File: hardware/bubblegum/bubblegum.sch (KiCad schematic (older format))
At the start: 136 parts, among them P1 RX_OUT, P2 RX_ONLY, P3 SERIAL, P4 TX/RX, P5 CONN_2, P6 TX_IN, P7 VCC, P8 SWITCH_CTRL, T1 RX_IF_BALUN, T2 RX_BALUN, T4 TX_BALUN, T6 TX_IF_BALUN, U1 DMN2400, U10 TX_HIGHPASS_FILTER, U11 PE4140, U12 SKY13350, U13 TX_LOWPASS_FILTER, U14 DMC2400, U15 DMC2400, U16 GSG-74HC04, U17 SKY13350, U18 DMN2400, U19 NCP699, U2 SKY13350, U3 RX_HIGHPASS_FILTER, U4 SKY13350, U5 SKY13350, U6 PE4140, U7 RX_LOWPASS_FILTER, U8 SKY13350, U9 TRF3765

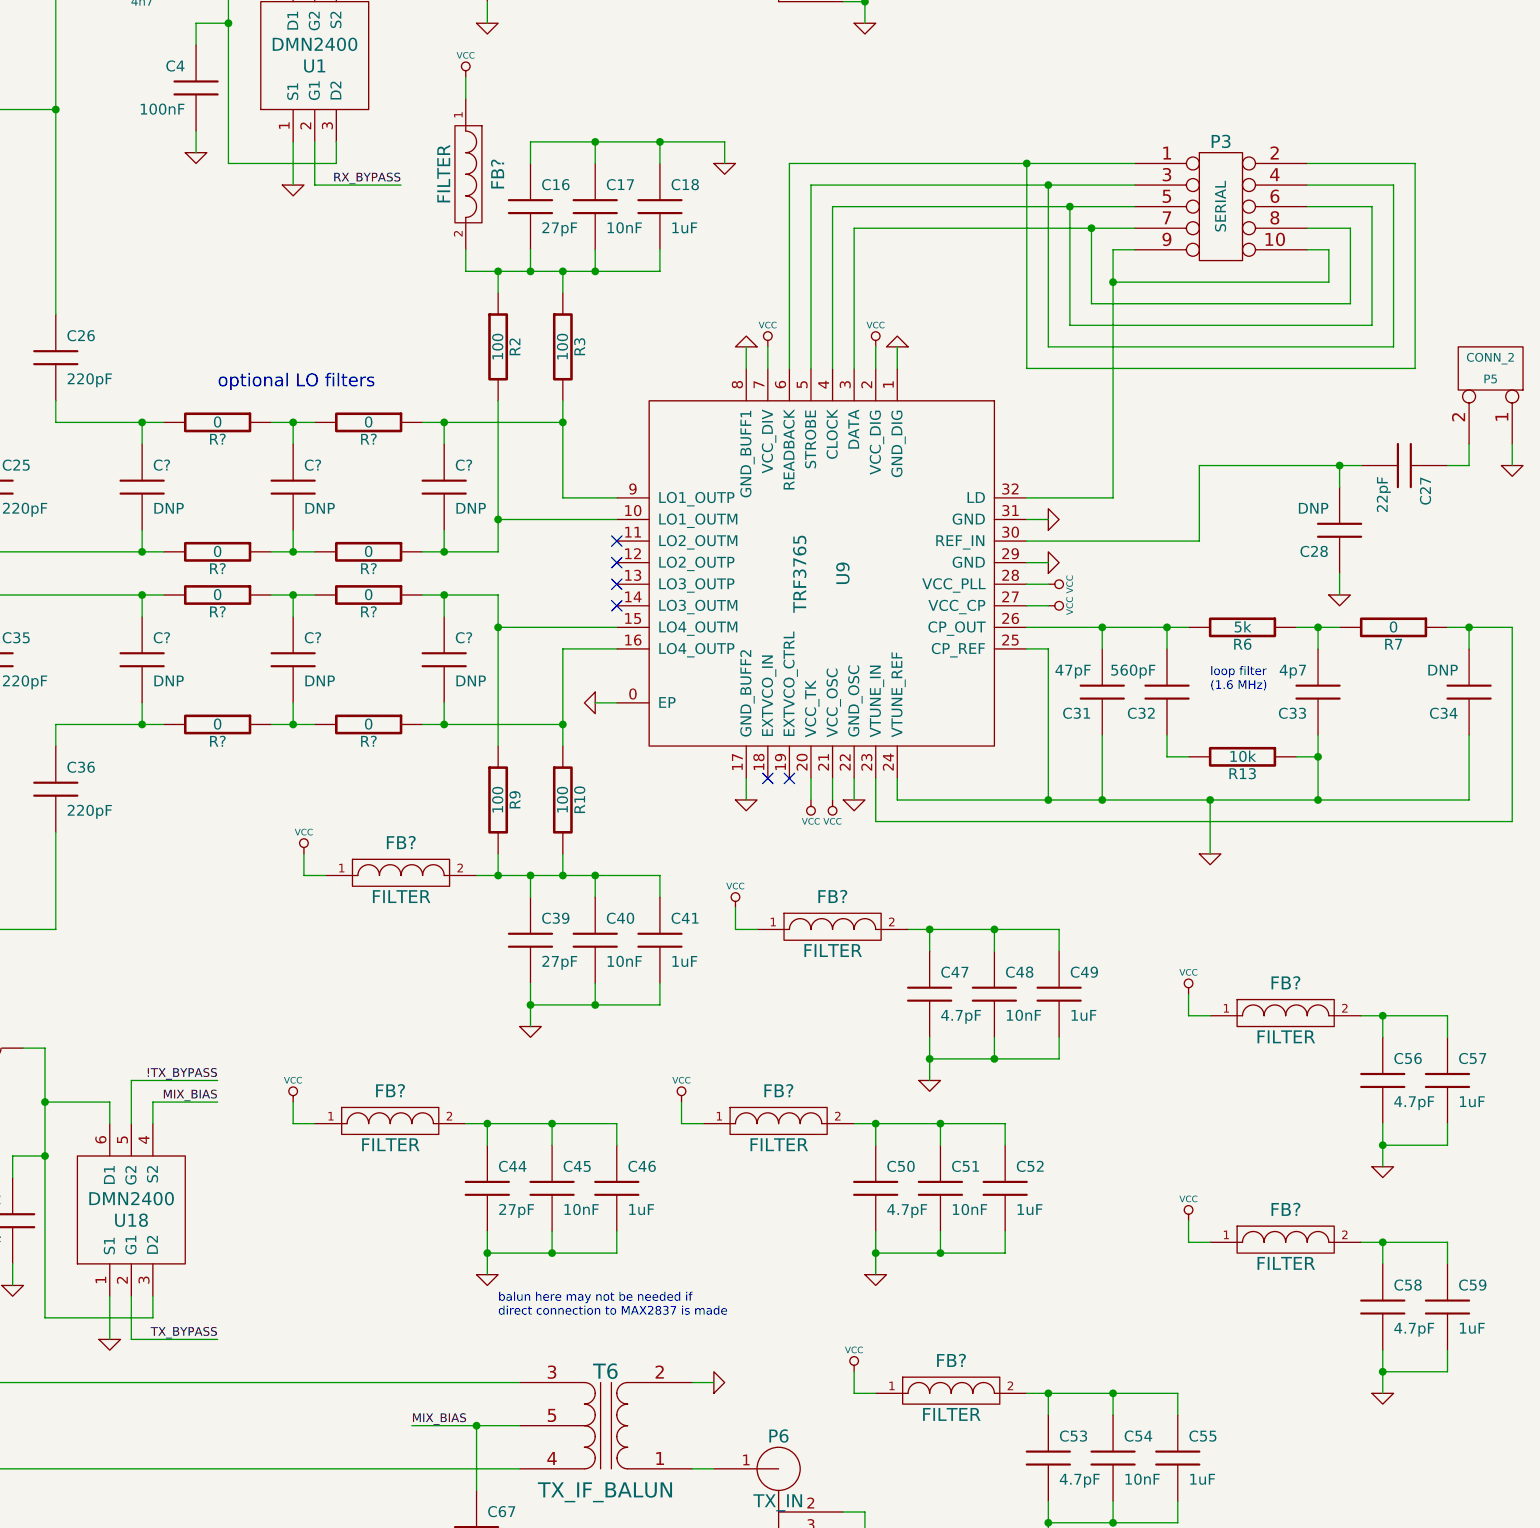
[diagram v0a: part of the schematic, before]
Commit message: started module selection, Anaren balun module
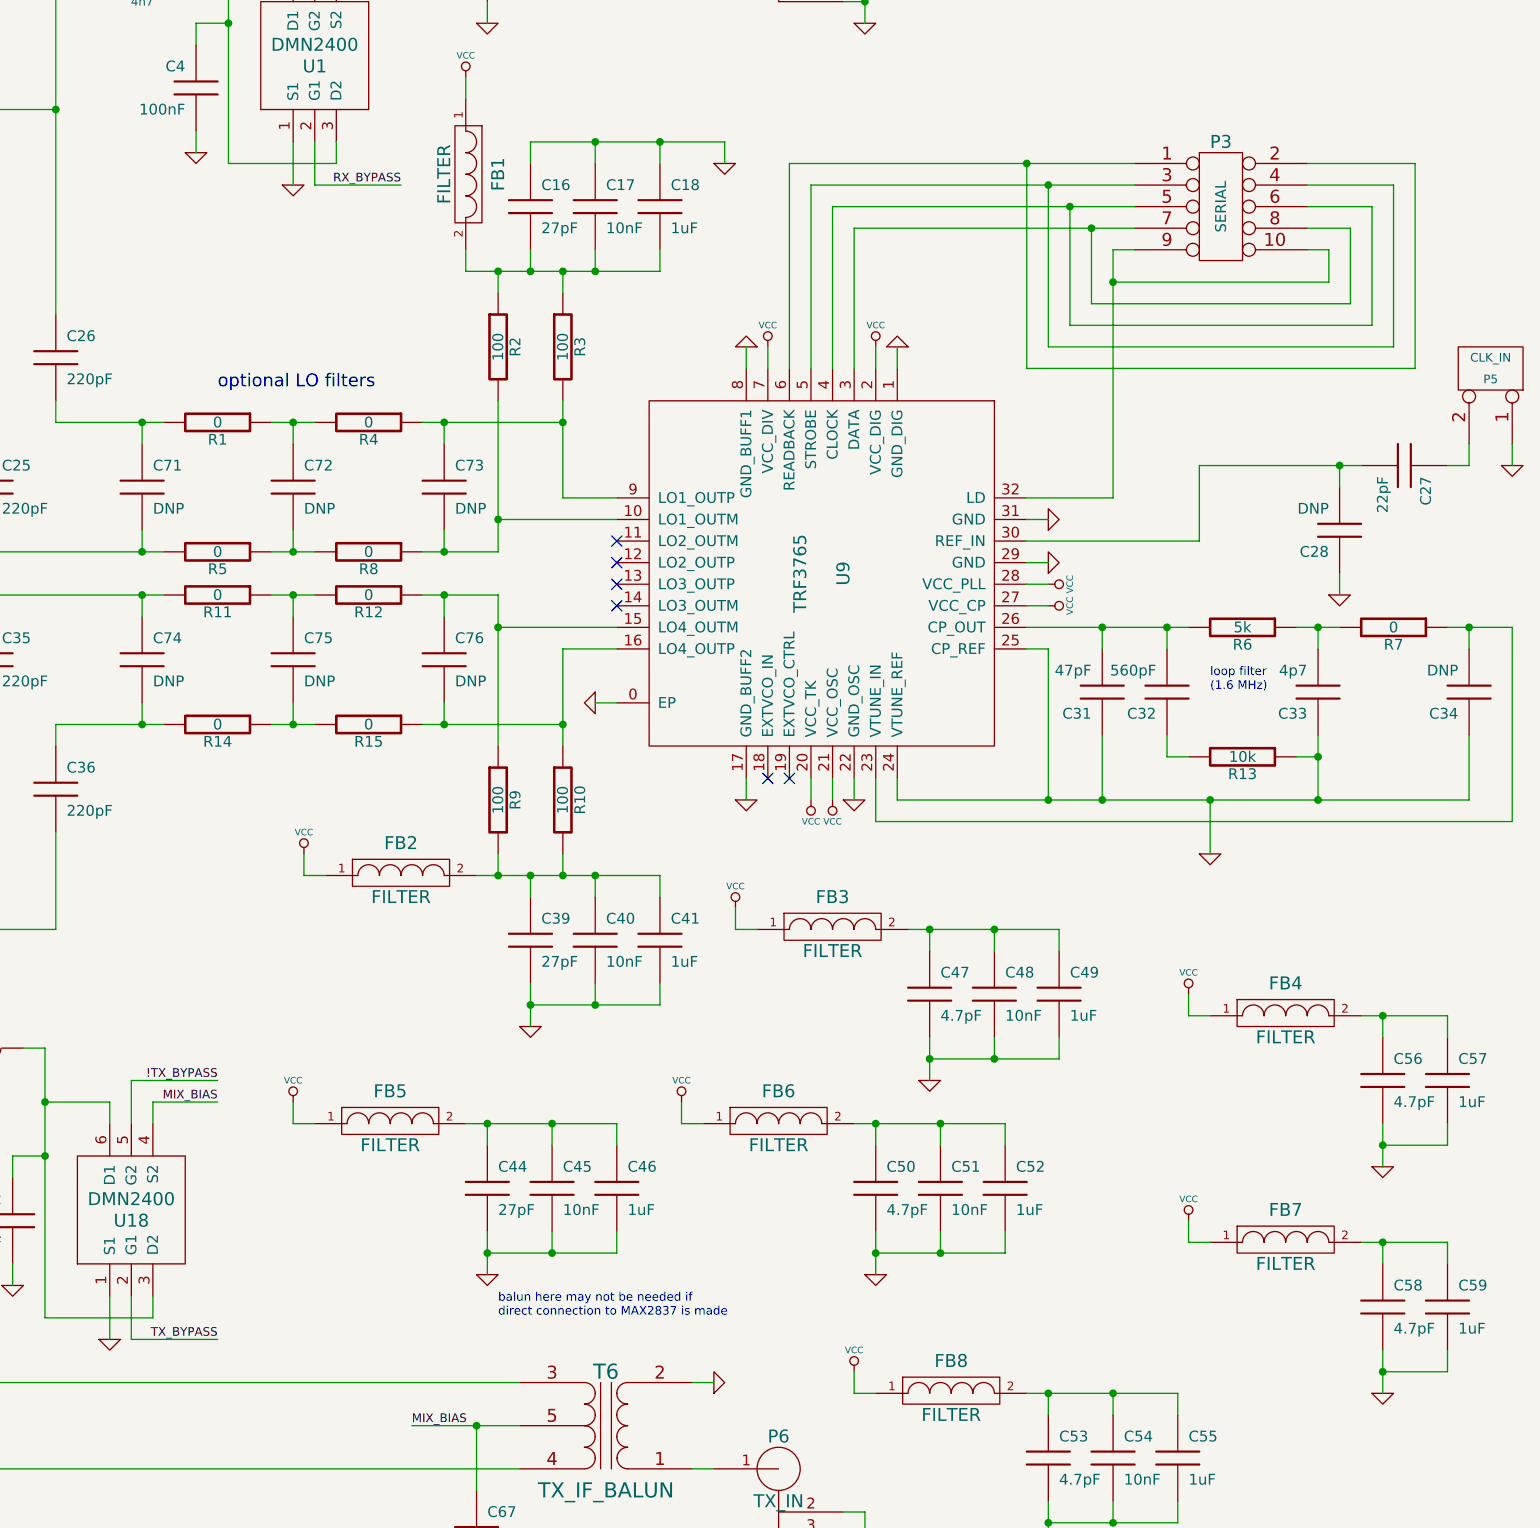
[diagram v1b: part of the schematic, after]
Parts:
- P5: value CONN_2 -> CLK_IN
- T1, T6: Description (none) -> BALUN CERAMIC CHIP WIMAX 2.5GHZ; Manufacturer (none) -> Johanson Technology; Part Number (none) -> 2500BL14M100T
- gave numbers to parts that had none: 22

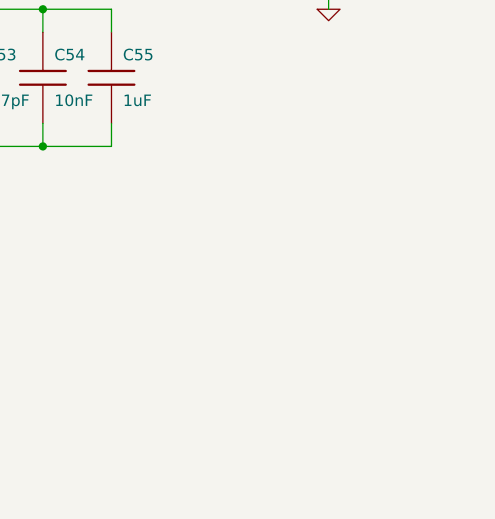
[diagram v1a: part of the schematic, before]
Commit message: mounting holes
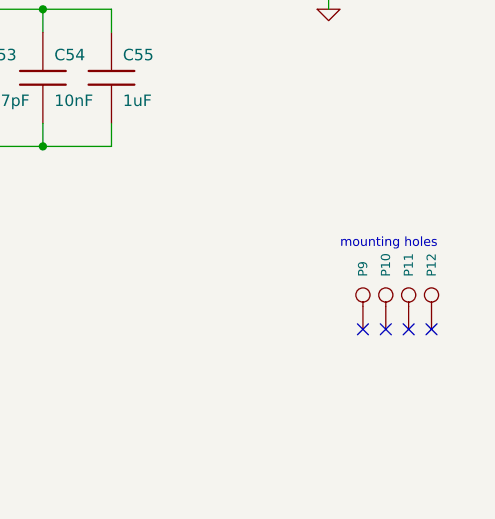
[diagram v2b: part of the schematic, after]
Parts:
- added P10, P11, P12, P9: CONN_1, symbol CONN_1
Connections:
- no-connect marks 7 -> 11
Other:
- note added: "mounting holes"

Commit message: fixed TRF3765 supply connections
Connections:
- net VCC: no longer U9.2 (VCC_DIG), U9.20 (VCC_TK), U9.21 (VCC_OSC), U9.27 (VCC_CP), U9.28 (VCC_PLL), U9.7 (VCC_DIV)
- net VCC_DIG: now reaches C44.1, C45.1, C46.1, FB5.2
- net VCC_DIG: now also U9.2 (VCC_DIG)
- net VCC_DIV: now reaches C47.1, C48.1, C49.1, FB3.2
- net VCC_DIV: now also U9.7 (VCC_DIV)
- net VCC_TK: now reaches C50.1, C51.1, C52.1, FB6.2
- net VCC_TK: now also U9.20 (VCC_TK)
- net VCC_CP: now reaches C58.1, C59.1, FB7.2
- net VCC_CP: now also U9.27 (VCC_CP)
- net VCC_PLL: now reaches C56.1, C57.1, FB4.2
- net VCC_PLL: now also U9.28 (VCC_PLL)
- net VCC_OSC: now reaches C53.1, C54.1, C55.1, FB8.2
- net VCC_OSC: now also U9.21 (VCC_OSC)
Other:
- moved on the sheet: C44, C45, C46, FB5

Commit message: switchable TX LO LPF
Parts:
- removed C74, C75, C76: DNP, symbol C
- removed R11, R12, R14, R15: 0, symbol R
- added C? (x4): 220pF, symbol C
- added C? (x2): 33pF, symbol C
- added T?: TX_LO_BALUN1, symbol BALUN-B0310J50100AHF
- added T?: TX_LO_BALUN2, symbol BALUN-B0310J50100AHF
- added U?: TX_LO_FILTER, symbol FIL-DEA
- added U?: SKY13411, symbol SKY13411
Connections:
- net GND: now also C?.2, C?.2, T?.1 (S1), T?.2 (S2), U?.0 (GND), U?.2 (GND), U?.4 (GND)
- net at R9.1, U9.15 (LO4_OUTM): now also C?.2
- net at R10.1, U9.16 (LO4_OUTP): now also C?.2
- net at C35.1: now also T?.3 (PR1)
- net at C36.1: now also T?.4 (PR2)
- new net: T?.1 (S1), U?.4 (TX)
- new net: C?.1, T?.3 (PR1)
- new net: C?.1, T?.4 (PR2)
- new net: C?.2, U?.1 (IN)
- new net: C?.1, U?.3 (OUT)
- new net: T?.2 (S2), U?.6 (ANT1)
- new net: C?.1, U?.1 (ANT2)
- new net: C?.2, U?.3 (RX)
- new net !TX_LO_LPF: C?.1, U?.2 (V2)
- new net TX_LO_LPF: C?.1, U?.5 (V1)
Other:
- moved on the sheet: C1, C10, C11, C12, C13, C15, C2, C20, C23, C24, C35, C36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

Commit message: finished switchable LO LPFs in schematic
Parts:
- removed P8: SWITCH_CTRL, symbol CONN_5X2
- removed R1, R4, R5, R8: 0, symbol R
- added C74: 33pF, symbol C
- added C75, C76: 220pF, symbol C
- added P8: SWITCH_CTRL, symbol CONN_7X2
- added T3: RX_LO_BALUN2, symbol BALUN-B0310J50100AHF
- added T5: RX_LO_BALUN1, symbol BALUN-B0310J50100AHF
- added U20: RX_LO_FILTER, symbol FIL-DEA
- added U21: SKY13411, symbol SKY13411
- C71, C72: value DNP -> 220pF
- C73: value DNP -> 33pF
- gave numbers to parts that had none: 10
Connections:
- net !TX_LO_LPF is gone; now on net !LO_LPF: C80.1, U22.2 (V2)
- net GND: now also C73.2, C74.2, P8.10, P8.12, P8.14, P8.2 (P2), P8.4 (P4), P8.6 (P6), P8.8 (P8), T3.1 (S1), T5.2 (S2), U20.2 (GND), U20.4 (GND), U21.0 (GND)
- net RX_BYPASS: now also P8.1 (P1)
- net RX_HP: now also P8.5 (P5)
- net TX_ANT: now also P8.9
- net TX_BYPASS: now also P8.3 (P3)
- net TX_HP: now also P8.7 (P7)
- net VCC: now also P8.13; no longer U16.13 (6A)
- net at R2.2, U9.10 (LO1_OUTM): now also C76.2; no longer C73.2
- net at R3.2, U9.9 (LO1_OUTP): now also C75.2; no longer C73.1
- net at C25.2: now also T3.4 (PR2); no longer C71.2
- net at C26.2: now also T3.3 (PR1); no longer C71.1
- net !LO_LPF: now reaches U16.12 (6Y)
- net !LO_LPF: now also C74.1, U21.2 (V2)
- net at C72.1: now also U20.3 (OUT)
- net at C72.2: now also U21.4 (TX)
- net TX_LO_LPF renamed LO_LPF
- net LO_LPF: now also C73.1, U16.13 (6A), P8.11, U21.5 (V1)
- new net: T3.2 (S2), U21.1 (ANT2)
- new net: C76.1, T5.3 (PR1)
- new net: C75.1, T5.4 (PR2)
- new net: T5.1 (S1), U21.3 (RX)
- new net: C71.1, U21.6 (ANT1)
- new net: C71.2, U20.1 (IN)
- no-connect marks 11 -> 10
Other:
- note removed: "optional LO filters"
- moved on the sheet: C10, C23, C25, C26, C3, C4, C77, C78, C79, C80, C81, C82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

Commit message: duplicated smallest LO supply caps
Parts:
- removed P3: SERIAL, symbol CONN_5X2
- added C83, C84: 27pF, symbol C
- added P3: SERIAL, symbol CONN_7X2
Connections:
- net GND: now also C83.1, C84.2, P3.1 (P1), P3.13, P3.14, P3.2 (P2)
- net at U9.3 (DATA): now also P3.10, P3.9
- net at U9.32 (LD): now also P3.11, P3.12
- net at U9.4 (CLOCK): now also P3.7 (P7), P3.8 (P8)
- net at U9.5 (STROBE): now also P3.5 (P5), P3.6 (P6)
- net at U9.6 (READBACK): now also P3.3 (P3), P3.4 (P4)
- net at C16.2, C17.2, C18.2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: now also C83.2
- net at C39.1, C40.1, C41.1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: now also C84.1
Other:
- moved on the sheet: C17, C18, FB2
